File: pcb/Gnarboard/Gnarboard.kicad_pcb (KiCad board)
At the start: 2 copper layers, 155 x 130 mm, 134 parts, among them J1 N2K, J10 Screw_Terminal_01x02, J11 Screw_Terminal_01x02, J12 Screw_Terminal_01x02, J2 I2C, J3 Screw_Terminal_01x12, J4 Screw_Terminal_01x12, J5 Screw_Terminal_01x02, J6 Screw_Terminal_01x02, J7 Screw_Terminal_01x02, J8 Screw_Terminal_01x02, J9 Screw_Terminal_01x02, Q1 MMBT5551L, Q10 IRF4905, Q11 MMBT5551L, Q12 IRF4905, Q13 MMBT5551L, Q14 IRF4905, Q15 MMBT5551L, Q16 IRF4905, Q2 IRF4905, Q3 MMBT5551L, Q4 IRF4905, Q5 MMBT5551L, Q6 IRF4905, Q7 MMBT5551L, Q8 IRF4905, Q9 MMBT5551L, U1 ESP32-DEVKITC, U10 ACS725xLCTR-20AU, U11 ACS725xLCTR-20AU, U12 ACS725xLCTR-20AU, U2 MCP3208, U4 D24V5F3, U5 ACS725xLCTR-20AU, U6 ACS725xLCTR-20AU, U7 ACS725xLCTR-20AU, U8 ACS725xLCTR-20AU, U9 ACS725xLCTR-20AU

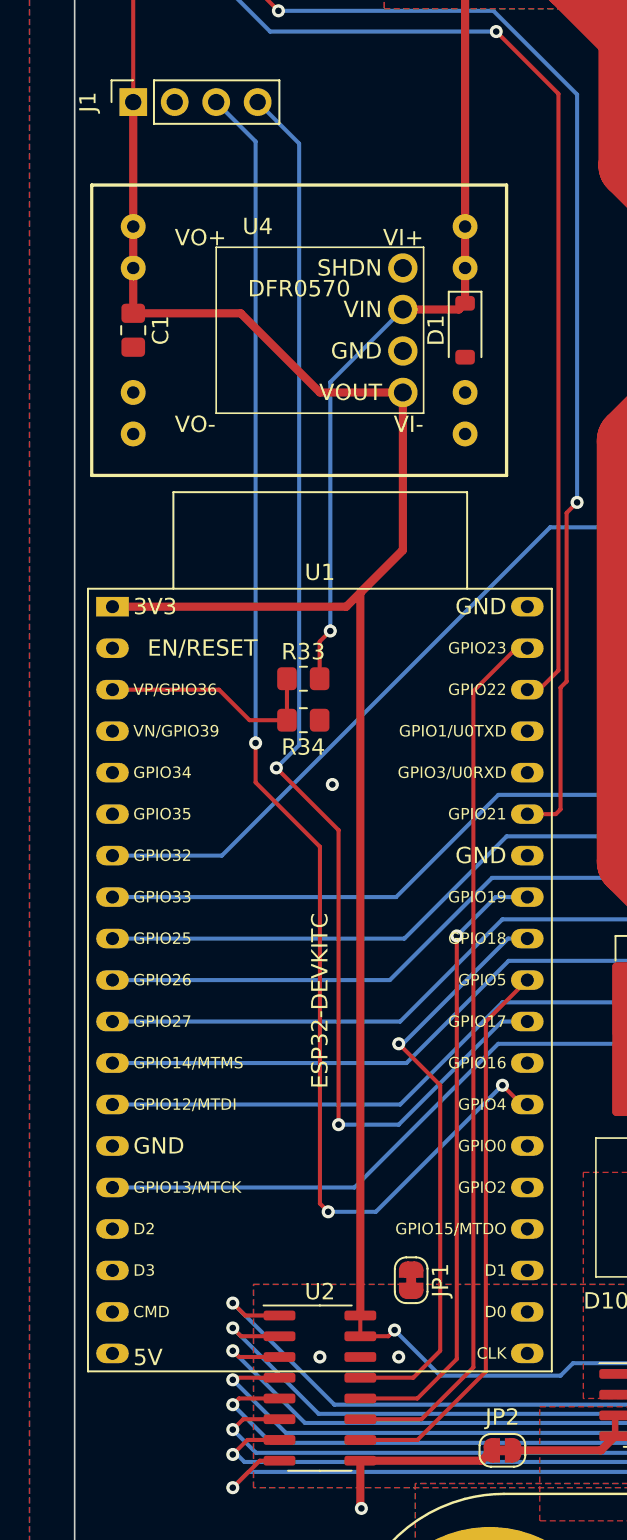
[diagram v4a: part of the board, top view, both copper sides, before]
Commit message: updated the pin selections and changed back to using a 5v regulator.
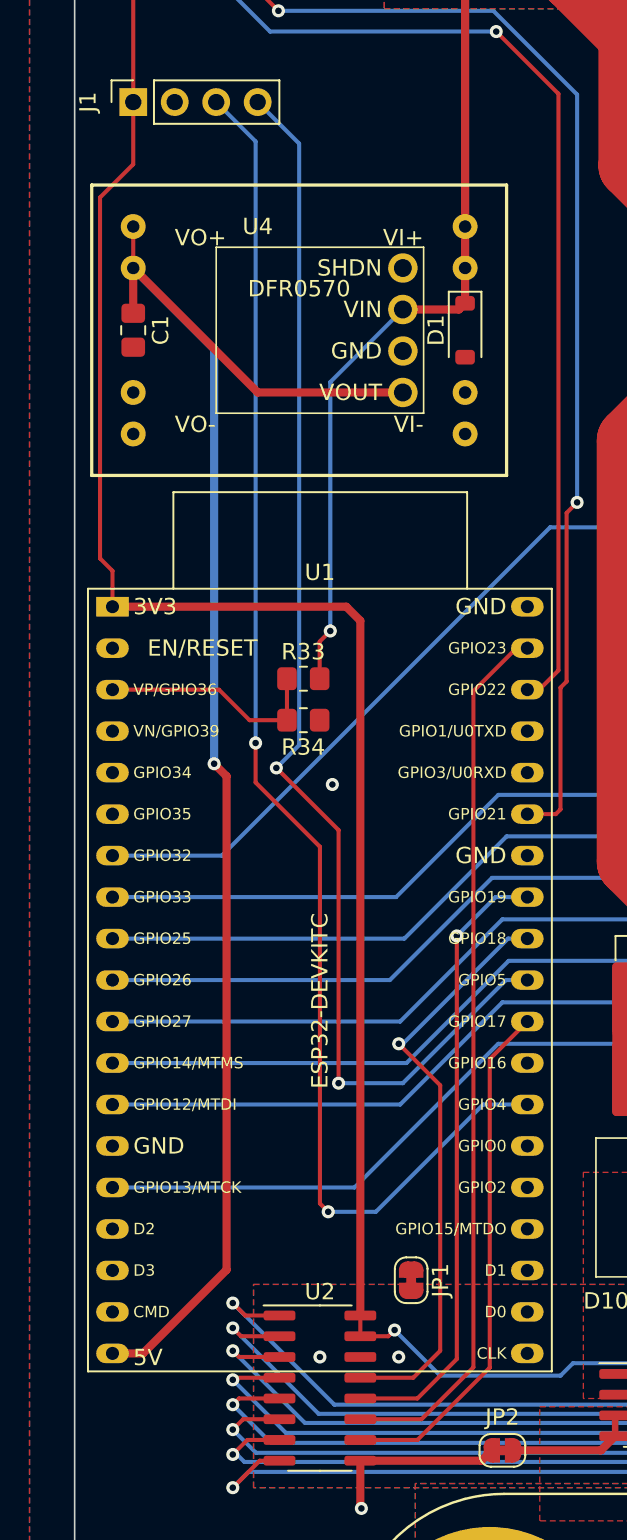
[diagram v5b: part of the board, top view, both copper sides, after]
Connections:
- C1 pad 1: +3.3V -> +5V
- DFR0570 pad 1: +3.3V -> +5V
- DFR0570 pad 2: +3.3V -> +5V
- U1 pad 19: unconnected-(U1-5V0-Pad19) -> +5V
- U1 pad 28: CAN_TX -> Net-(U1-GPIO17)
- U1 pad 29: Net-(U1-GPIO5) -> CAN_TX
- U2 pad 10: Net-(U1-GPIO5) -> Net-(U1-GPIO17)
- U4 pad 4: +3.3V -> +5V
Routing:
- net +5V: track 0.00 -> 97.8 mm, vias 0 -> 1
- net Net-(U1-GPIO5): track 34.4 -> 0.00 mm
- net Net-(U1-GPIO17): track 0.00 -> 31.9 mm
- net +3.3V: track 290.0 -> 271.9 mm
- net CAN_TX: track 80.0 -> 77.5 mm
- net CAN_RX: track 86.7 -> 86.0 mm, vias 3 -> 2

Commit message: a couple tweaks to the board
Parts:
- D1: footprint Diode_SMD:D_SOD-123 -> Diode_SMD:D_SOD-123F

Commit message: went over components again, should be ready to rock and roll!
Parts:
- removed DFR0570: ~, gnarboard:DF1768
- added DFR0571: ~, gnarboard:DF1768, F.Cu at (74.9, 63.5)
- Q1, Q11, Q13, Q15, Q3, Q5, Q7, Q9: value MMBT5551L -> BC817

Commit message: pcb stuff
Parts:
- D10, D11, D12, D13, D14, D15, D16, D17: value GS1G-LTP -> SS16
- J10, J11, J12, J5, J6, J7, J8, J9: footprint gnarboard:Amphenol OQ02715 -> gnarboard:Molex 1x02 .375
- R11, R15, R19, R23, R27, R3, R31, R7: value 33k -> 22k
- R12, R16, R20, R24, R28, R32, R4, R8: value 6.8k -> 4.7k
- moved J1 92.7 mm to (66.0, 142.2), turned to 180 degrees
- moved J2 87.6 mm to (65.8, 127.0)
- moved R34 40.3 mm to (88.9, 49.5)
- moved R33 40.3 mm to (88.9, 47.0)
- moved C1 39.4 mm to (64.8, 102.9), turned to 0 degrees
- moved U12 35.1 mm to (234.1, 115.6)
- moved C26 34.4 mm to (241.9, 116.3)
- moved C24 34.4 mm to (241.9, 118.9)
- moved C25 34.4 mm to (241.9, 113.8)
- moved J12 33.6 mm to (234.4, 133.0), turned to 0 degrees
- moved U11 31.4 mm to (215.0, 115.6)
- moved C21 30.6 mm to (222.8, 118.9)
- moved C23 30.6 mm to (222.8, 116.3)
- moved C22 30.6 mm to (222.8, 113.8)
- moved J11 30.1 mm to (215.4, 133.0), turned to 0 degrees
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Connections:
- D10 pad 2: Net-(D10-A) -> GNDPWR
- D11 pad 2: Net-(D11-A) -> GNDPWR
- D12 pad 2: Net-(D12-A) -> GNDPWR
- D13 pad 2: Net-(D13-A) -> GNDPWR
- D14 pad 2: Net-(D14-A) -> GNDPWR
- D15 pad 2: Net-(D15-A) -> GNDPWR
- D16 pad 2: Net-(D16-A) -> GNDPWR
- D17 pad 2: Net-(D17-A) -> GNDPWR
- F1 pad 3: Net-(D10-K) -> Net-(Q2-D)
- F2 pad 3: Net-(D11-K) -> Net-(Q4-D)
- F3 pad 3: Net-(D12-K) -> Net-(Q6-D)
- F4 pad 3: Net-(D13-K) -> Net-(Q8-D)
- F5 pad 3: Net-(D14-K) -> Net-(Q10-D)
- F6 pad 3: Net-(D15-K) -> Net-(Q12-D)
- F7 pad 3: Net-(D16-K) -> Net-(Q14-D)
- F8 pad 3: Net-(D17-K) -> Net-(Q16-D)
- J10 pad 2: Net-(D15-A) -> GNDPWR
- J11 pad 2: Net-(D16-A) -> GNDPWR
- J12 pad 2: Net-(D17-A) -> GNDPWR
- J5 pad 2: Net-(D10-A) -> GNDPWR
- J6 pad 2: Net-(D11-A) -> GNDPWR
- J7 pad 2: Net-(D12-A) -> GNDPWR
- J8 pad 2: Net-(D13-A) -> GNDPWR
- J9 pad 2: Net-(D14-A) -> GNDPWR
- Q10 pad 2: Net-(D14-K) -> Net-(Q10-D)
- Q12 pad 2: Net-(D15-K) -> Net-(Q12-D)
- Q14 pad 2: Net-(D16-K) -> Net-(Q14-D)
- Q16 pad 2: Net-(D17-K) -> Net-(Q16-D)
- Q2 pad 2: Net-(D10-K) -> Net-(Q2-D)
- Q4 pad 2: Net-(D11-K) -> Net-(Q4-D)
- Q6 pad 2: Net-(D12-K) -> Net-(Q6-D)
- Q8 pad 2: Net-(D13-K) -> Net-(Q8-D)
- U10 pad 1: Net-(D15-A) -> Net-(Q12-D)
- U10 pad 2: Net-(D15-A) -> Net-(Q12-D)
- U10 pad 3: GNDPWR -> Net-(D15-K)
- U10 pad 4: GNDPWR -> Net-(D15-K)
- U11 pad 1: Net-(D16-A) -> Net-(Q14-D)
- U11 pad 2: Net-(D16-A) -> Net-(Q14-D)
- U11 pad 3: GNDPWR -> Net-(D16-K)
- U11 pad 4: GNDPWR -> Net-(D16-K)
- U12 pad 1: Net-(D17-A) -> Net-(Q16-D)
- U12 pad 2: Net-(D17-A) -> Net-(Q16-D)
- U12 pad 3: GNDPWR -> Net-(D17-K)
- U12 pad 4: GNDPWR -> Net-(D17-K)
- U5 pad 1: Net-(D10-A) -> Net-(Q2-D)
- U5 pad 2: Net-(D10-A) -> Net-(Q2-D)
- U5 pad 3: GNDPWR -> Net-(D10-K)
- U5 pad 4: GNDPWR -> Net-(D10-K)
- U6 pad 1: Net-(D11-A) -> Net-(Q4-D)
- U6 pad 2: Net-(D11-A) -> Net-(Q4-D)
- U6 pad 3: GNDPWR -> Net-(D11-K)
- U6 pad 4: GNDPWR -> Net-(D11-K)
- U7 pad 1: Net-(D12-A) -> Net-(Q6-D)
- U7 pad 2: Net-(D12-A) -> Net-(Q6-D)
- U7 pad 3: GNDPWR -> Net-(D12-K)
- U7 pad 4: GNDPWR -> Net-(D12-K)
- U8 pad 1: Net-(D13-A) -> Net-(Q8-D)
- U8 pad 2: Net-(D13-A) -> Net-(Q8-D)
- U8 pad 3: GNDPWR -> Net-(D13-K)
- U8 pad 4: GNDPWR -> Net-(D13-K)
- U9 pad 1: Net-(D14-A) -> Net-(Q10-D)
- U9 pad 2: Net-(D14-A) -> Net-(Q10-D)
- U9 pad 3: GNDPWR -> Net-(D14-K)
- U9 pad 4: GNDPWR -> Net-(D14-K)
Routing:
- net +24V: track 733.6 -> 0.00 mm, vias 9 -> 0
- net +3.3V: track 271.9 -> 0.00 mm, vias 9 -> 0
- net /PWM7: track 161.1 -> 0.00 mm, vias 1 -> 0
- net /ADC7: track 146.7 -> 0.00 mm, vias 2 -> 0
- net /PWM6: track 144.0 -> 0.00 mm, vias 1 -> 0
- net /ADC6: track 131.0 -> 0.00 mm, vias 2 -> 0
- net /PWM5: track 127.9 -> 0.00 mm, vias 1 -> 0
- net /ADC5: track 118.8 -> 0.00 mm, vias 2 -> 0
- net /PWM4: track 111.8 -> 0.00 mm, vias 1 -> 0
- net /ADC4: track 101.0 -> 0.00 mm, vias 2 -> 0
- net +5V: track 97.8 -> 0.00 mm, vias 1 -> 0
- net /PWM3: track 95.8 -> 0.00 mm, vias 1 -> 0
- net /ADC3: track 86.1 -> 0.00 mm, vias 2 -> 0
- net CAN_RX: track 86.0 -> 0.00 mm, vias 2 -> 0
- net Net-(D11-K): track 84.4 -> 0.00 mm
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- added copper zone on F.Cu, net Net-(D10-K)
- added copper zone on F.Cu, net Net-(D11-K)
- added copper zone on F.Cu, net Net-(D12-K)
- added copper zone on F.Cu, net Net-(D13-K)
- added copper zone on F.Cu, net Net-(D14-K)
- added copper zone on F.Cu, net Net-(D15-K)
- added copper zone on F.Cu, net Net-(D16-K)
- added copper zone on F.Cu, net Net-(D17-K)
- added copper zone on F.Cu, net Net-(Q10-D)
- added copper zone on F.Cu, net Net-(Q10-S)
- added copper zone on F.Cu, net Net-(Q12-D)
- added copper zone on F.Cu, net Net-(Q12-S)
- added copper zone on F.Cu, net Net-(Q14-D)
- added copper zone on F.Cu, net Net-(Q14-S)
- added copper zone on F.Cu, net Net-(Q16-D)
- added copper zone on F.Cu, net Net-(Q16-S)
- added copper zone on F.Cu, net Net-(Q2-D)
- added copper zone on F.Cu, net Net-(Q2-S)
- added copper zone on F.Cu, net Net-(Q4-D)
- added copper zone on F.Cu, net Net-(Q4-S)
- added copper zone on F.Cu, net Net-(Q6-D)
- added copper zone on F.Cu, net Net-(Q6-S)
- added copper zone on F.Cu, net Net-(Q8-D)
- added copper zone on F.Cu, net Net-(Q8-S)
- removed copper zone on F.Cu, net Net-(D10-A)
- removed copper zone on F.Cu, net Net-(D11-A)
- removed copper zone on F.Cu, net Net-(D12-A)
- removed copper zone on F.Cu, net Net-(D13-A)
- removed copper zone on F.Cu, net Net-(D14-A)
- removed copper zone on F.Cu, net Net-(D15-A)
- removed copper zone on F.Cu, net Net-(D16-A)
- removed copper zone on F.Cu, net Net-(D17-A)
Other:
- board size 155 x 130 mm -> 184 x 136 mm
